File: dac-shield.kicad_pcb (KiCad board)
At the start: 2 copper layers, 53.3 x 53.3 mm, 40 parts, among them J1 Conn_01x02, J2 Conn_01x02, J3 Conn_01x02, J4 Conn_01x02, J5 Conn_01x02, J6 Conn_01x02, J7 Conn_01x02, J8 Conn_01x02

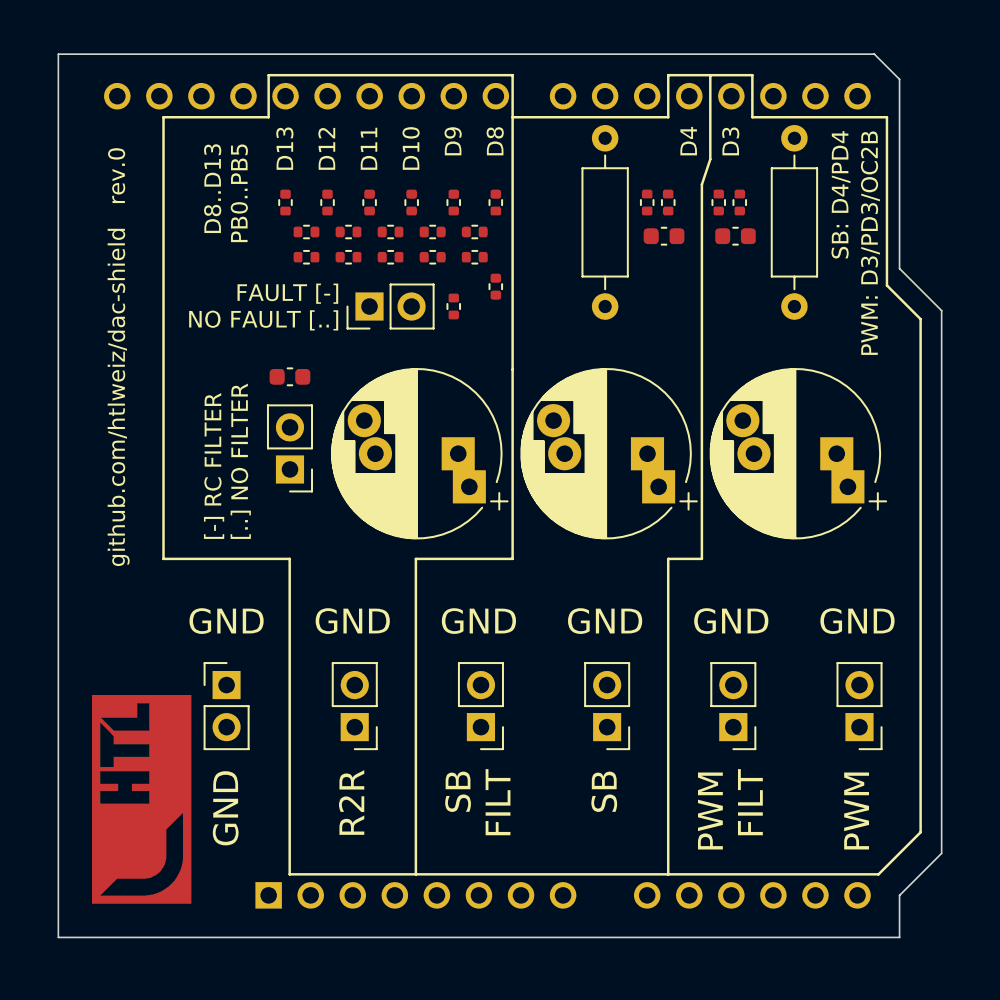
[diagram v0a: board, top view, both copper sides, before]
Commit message: modified silkscreen
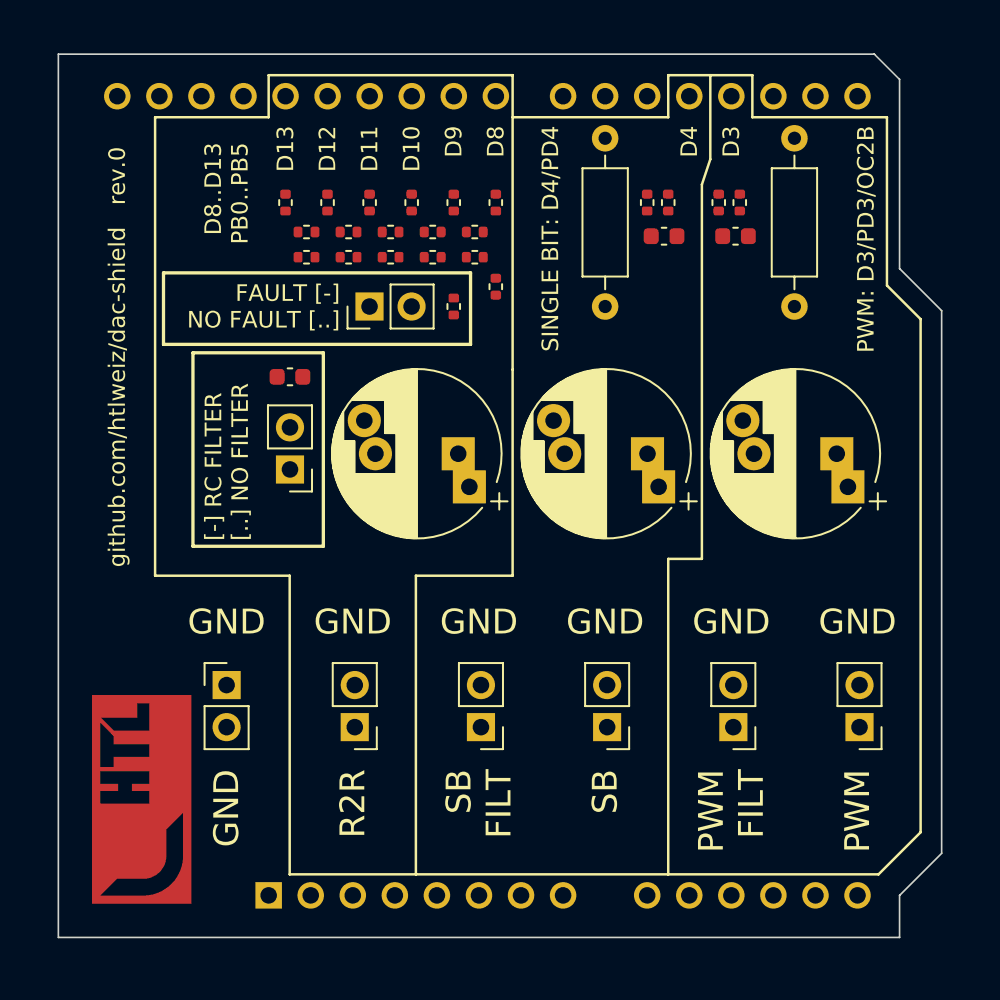
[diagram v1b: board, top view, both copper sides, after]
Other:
- board text added: "SINGLE BIT: D4/PD4"
- board text removed: "SB: D4/PD4"
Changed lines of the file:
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@@
   (gr_line (start 146.05 77.47) (end 148.59 77.47) (layer "F.SilkS") (width 0.15))
   (gr_line (start 161.29 92.202) (end 161.29 123.19) (layer "F.SilkS") (width 0.15))
-  (gr_line (start 136.652 106.68) (end 130.81 106.68) (layer "F.SilkS") (width 0.15))
+  (gr_line (start 136.652 107.696) (end 130.81 107.696) (layer "F.SilkS") (width 0.15))
   (gr_line (start 161.29 123.19) (end 158.75 125.73) (layer "F.SilkS") (width 0.15))
-  (gr_line (start 123.19 125.73) (end 123.19 106.68) (layer "F.SilkS") (width 0.15))
-  (gr_line (start 123.19 106.68) (end 115.57 106.68) (layer "F.SilkS") (width 0.15))
-  (gr_line (start 130.81 106.68) (end 130.81 125.73) (layer "F.SilkS") (width 0.15))
+  (gr_line (start 123.19 125.73) (end 123.19 107.696) (layer "F.SilkS") (width 0.15))
+  (gr_rect (start 115.57 89.408) (end 134.112 93.726) (layer "F.SilkS") (width 0.2) (fill none))
+  (gr_line (start 123.19 107.696) (end 115.062 107.696) (layer "F.SilkS") (width 0.15))
+  (gr_line (start 130.81 107.696) (end 130.81 125.73) (layer "F.SilkS") (width 0.15))
   (gr_line (start 158.75 125.73) (end 146.05 125.73) (layer "F.SilkS") (width 0.15))
   (gr_line (start 151.13 80.01) (end 159.258 80.01) (layer "F.SilkS") (width 0.15))
   (gr_line (start 159.258 90.17) (end 161.29 92.202) (layer "F.SilkS") (width 0.15))
   (gr_line (start 148.59 77.47) (end 148.59 82.55) (layer "F.SilkS") (width 0.15))
+  (gr_rect (start 117.348 105.918) (end 125.222 94.234) (layer "F.SilkS") (width 0.2) (fill none))
   (gr_line (start 136.652 77.47) (end 121.92 77.47) (layer "F.SilkS") (width 0.15))
   (gr_line (start 146.05 77.47) (end 146.05 80.01) (layer "F.SilkS") (width 0.15))
   (gr_line (start 146.05 106.68) (end 146.05 125.73) (layer "F.SilkS") (width 0.15))
-  (gr_line (start 115.57 80.01) (end 121.92 80.01) (layer "F.SilkS") (width 0.15))
-  (gr_line (start 136.652 95.25) (end 136.652 106.68) (layer "F.SilkS") (width 0.15))
-  (gr_line (start 115.57 106.68) (end 115.57 80.01) (layer "F.SilkS") (width 0.15))
+  (gr_line (start 115.062 80.01) (end 121.92 80.01) (layer "F.SilkS") (width 0.15))
+  (gr_line (start 136.652 95.25) (end 136.652 107.696) (layer "F.SilkS") (width 0.15))
+  (gr_line (start 115.062 107.696) (end 115.062 80.01) (layer "F.SilkS") (width 0.15))
   (gr_line (start 159.258 80.01) (end 159.258 90.17) (layer "F.SilkS") (width 0.15))
   (gr_line (start 148.082 106.68) (end 146.05 106.68) (layer "F.SilkS") (width 0.15))
@@
     (effects (font (size 1 1) (thickness 0.16)) (justify right))
   )
-  (gr_text "PWM: D3/PD3/OC2B" (at 158.242 80.772 90) (layer "F.SilkS")
+  (gr_text "PWM: D3/PD3/OC2B" (at 157.988 80.518 90) (layer "F.SilkS")
     (effects (font (size 1 1) (thickness 0.16)) (justify right))
   )
@@
     (effects (font (size 1 1) (thickness 0.16)) (justify right))
   )
-  (gr_text "SB: D4/PD4" (at 156.464 80.772 90) (layer "F.SilkS")
+  (gr_text "SINGLE BIT: D4/PD4" (at 138.938 80.518 90) (layer "F.SilkS")
     (effects (font (size 1 1) (thickness 0.16)) (justify right))
   )

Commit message: fixed cap value and added annotations
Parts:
- C1, C3, C5: value 16n -> 15n
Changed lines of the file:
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@@
   (net 31 "/pwm_filt")
   (net 32 "/sb_filt")
-  (net 33 "Net-(C6-Pad1)")
+  (net 33 "Net-(C5-Pad1)")
   (net 34 "Net-(J4-Pad1)")
   (net 35 "Net-(J4-Pad2)")
   (net 36 "/r2r_filt")
   (net 37 "Net-(R4-Pad2)")
-  (net 38 "Net-(R6-Pad2)")
-  (net 39 "Net-(R11-Pad2)")
+  (net 38 "Net-(R10-Pad1)")
+  (net 39 "Net-(R10-Pad2)")
   (net 40 "Net-(R19-Pad2)")
   (footprint "Resistor_SMD:R_0402_1005Metric" (layer "F.Cu")
@@
     (fp_circle (center 2.5 0) (end 7.5 0) (layer "F.Fab") (width 0.1) (fill none))
     (pad "1" thru_hole rect (at 0 0 180) (size 2 2) (drill 1) (layers *.Cu *.Mask)
-      (net 33 "Net-(C6-Pad1)") (pintype "passive"))
+      (net 33 "Net-(C5-Pad1)") (pintype "passive"))
     (pad "1" thru_hole rect (at -0.672144 -2 180) (size 2 2) (drill 1) (layers *.Cu *.Mask)
-      (net 33 "Net-(C6-Pad1)") (pintype "passive"))
+      (net 33 "Net-(C5-Pad1)") (pintype "passive"))
     (pad "2" thru_hole circle (at 5 0 180) (size 2 2) (drill 1) (layers *.Cu *.Mask)
       (net 6 "GND") (pintype "passive"))
@@
     (fp_line (start 0.525 0.27) (end -0.525 0.27) (layer "F.Fab") (width 0.1))
     (pad "1" smd roundrect (at -0.51 0 180) (size 0.54 0.64) (layers "F.Cu" "F.Paste" "F.Mask") (roundrect_rratio 0.25)
-      (net 39 "Net-(R11-Pad2)") (pintype "passive"))
+      (net 39 "Net-(R10-Pad2)") (pintype "passive"))
     (pad "2" smd roundrect (at 0.51 0 180) (size 0.54 0.64) (layers "F.Cu" "F.Paste" "F.Mask") (roundrect_rratio 0.25)
       (net 34 "Net-(J4-Pad1)") (pintype "passive"))
@@
       (effects (font (size 1 1) (thickness 0.15)))
     )
-    (fp_text value "16n" (at 0 1.43) (layer "F.Fab")
+    (fp_text value "15n" (at 0 1.43) (layer "F.Fab")
       (effects (font (size 1 1) (thickness 0.15)))
     )
@@
       (net 23 "/b1") (pintype "passive"))
     (pad "2" smd roundrect (at 0.51 0 270) (size 0.54 0.64) (layers "F.Cu" "F.Paste" "F.Mask") (roundrect_rratio 0.25)
-      (net 38 "Net-(R6-Pad2)") (pintype "passive"))
+      (net 38 "Net-(R10-Pad1)") (pintype "passive"))
     (model "${KICAD6_3DMODEL_DIR}/Resistor_SMD.3dshapes/R_0402_1005Metric.wrl"
       (offset (xyz 0 0 0))
@@
     (fp_line (start -0.525 0.27) (end -0.525 -0.27) (layer "F.Fab") (width 0.1))
     (pad "1" smd roundrect (at -0.51 0 270) (size 0.54 0.64) (layers "F.Cu" "F.Paste" "F.Mask") (roundrect_rratio 0.25)
-      (net 39 "Net-(R11-Pad2)") (pintype "passive"))
+      (net 39 "Net-(R10-Pad2)") (pintype "passive"))
     (pad "2" smd roundrect (at 0.51 0 270) (size 0.54 0.64) (layers "F.Cu" "F.Paste" "F.Mask") (roundrect_rratio 0.25)
       (net 35 "Net-(J4-Pad2)") (pintype "passive"))
@@
       (net 24 "/b2") (pintype "passive"))
     (pad "2" smd roundrect (at 0.51 0 270) (size 0.54 0.64) (layers "F.Cu" "F.Paste" "F.Mask") (roundrect_rratio 0.25)
-      (net 39 "Net-(R11-Pad2)") (pintype "passive"))
+      (net 39 "Net-(R10-Pad2)") (pintype "passive"))
     (model "${KICAD6_3DMODEL_DIR}/Resistor_SMD.3dshapes/R_0402_1005Metric.wrl"
       (offset (xyz 0 0 0))
@@
       (net 36 "/r2r_filt") (pinfunction "Pin_1") (pintype "passive"))
     (pad "2" thru_hole oval (at 0 2.54 180) (size 1.7 1.7) (drill 1) (layers *.Cu *.Mask)
-      (net 33 "Net-(C6-Pad1)") (pinfunction "Pin_2") (pintype "passive"))
+      (net 33 "Net-(C5-Pad1)") (pinfunction "Pin_2") (pintype "passive"))
     (model "${KICAD6_3DMODEL_DIR}/Connector_PinHeader_2.54mm.3dshapes/PinHeader_1x02_P2.54mm_Vertical.wrl"
       (offset (xyz 0 0 0))
@@
       (net 37 "Net-(R4-Pad2)") (pintype "passive"))
     (pad "2" smd roundrect (at 0.51 0 180) (size 0.54 0.64) (layers "F.Cu" "F.Paste" "F.Mask") (roundrect_rratio 0.25)
-      (net 38 "Net-(R6-Pad2)") (pintype "passive"))
+      (net 38 "Net-(R10-Pad1)") (pintype "passive"))
     (model "${KICAD6_3DMODEL_DIR}/Resistor_SMD.3dshapes/R_0402_1005Metric.wrl"
       (offset (xyz 0 0 0))
@@
     (fp_line (start 0.525 0.27) (end -0.525 0.27) (layer "F.Fab") (width 0.1))
     (pad "1" smd roundrect (at -0.51 0 180) (size 0.54 0.64) (layers "F.Cu" "F.Paste" "F.Mask") (roundrect_rratio 0.25)
-      (net 38 "Net-(R6-Pad2)") (pintype "passive"))
+      (net 38 "Net-(R10-Pad1)") (pintype "passive"))
     (pad "2" smd roundrect (at 0.51 0 180) (size 0.54 0.64) (layers "F.Cu" "F.Paste" "F.Mask") (roundrect_rratio 0.25)
-      (net 39 "Net-(R11-Pad2)") (pintype "passive"))
+      (net 39 "Net-(R10-Pad2)") (pintype "passive"))
     (model "${KICAD6_3DMODEL_DIR}/Resistor_SMD.3dshapes/R_0402_1005Metric.wrl"
       (offset (xyz 0 0 0))
@@
     (fp_line (start 0.525 0.27) (end -0.525 0.27) (layer "F.Fab") (width 0.1))
     (pad "1" smd roundrect (at -0.51 0 180) (size 0.54 0.64) (layers "F.Cu" "F.Paste" "F.Mask") (roundrect_rratio 0.25)
-      (net 38 "Net-(R6-Pad2)") (pintype "passive"))
+      (net 38 "Net-(R10-Pad1)") (pintype "passive"))
     (pad "2" smd roundrect (at 0.51 0 180) (size 0.54 0.64) (layers "F.Cu" "F.Paste" "F.Mask") (roundrect_rratio 0.25)
-      (net 39 "Net-(R11-Pad2)") (pintype "passive"))
+      (net 39 "Net-(R10-Pad2)") (pintype "passive"))
     (model "${KICAD6_3DMODEL_DIR}/Resistor_SMD.3dshapes/R_0402_1005Metric.wrl"
       (offset (xyz 0 0 0))
@@
       (effects (font (size 1 1) (thickness 0.15)))
     )
-    (fp_text value "16n" (at 0 1.43) (layer "F.Fab")
+    (fp_text value "15n" (at 0 1.43) (layer "F.Fab")
       (effects (font (size 1 1) (thickness 0.15)))
     )
@@
       (effects (font (size 1 1) (thickness 0.15)))
     )
-    (fp_text value "16n" (at 0 1.43) (layer "F.Fab")
+    (fp_text value "15n" (at 0 1.43) (layer "F.Fab")
       (effects (font (size 1 1) (thickness 0.15)))
     )
@@
     (fp_line (start 0.8 0.4) (end -0.8 0.4) (layer "F.Fab") (width 0.1))
     (pad "1" smd roundrect (at -0.775 0) (size 0.9 0.95) (layers "F.Cu" "F.Paste" "F.Mask") (roundrect_rratio 0.25)
-      (net 33 "Net-(C6-Pad1)") (pintype "passive"))
+      (net 33 "Net-(C5-Pad1)") (pintype "passive"))
     (pad "2" smd roundrect (at 0.775 0) (size 0.9 0.95) (layers "F.Cu" "F.Paste" "F.Mask") (roundrect_rratio 0.25)
       (net 6 "GND") (pintype "passive"))
@@
     (fp_line (start 0.525 -0.27) (end 0.525 0.27) (layer "F.Fab") (width 0.1))
     (pad "1" smd roundrect (at -0.51 0 180) (size 0.54 0.64) (layers "F.Cu" "F.Paste" "F.Mask") (roundrect_rratio 0.25)
-      (net 39 "Net-(R11-Pad2)") (pintype "passive"))
+      (net 39 "Net-(R10-Pad2)") (pintype "passive"))
     (pad "2" smd roundrect (at 0.51 0 180) (size 0.54 0.64) (layers "F.Cu" "F.Paste" "F.Mask") (roundrect_rratio 0.25)
       (net 34 "Net-(J4-Pad1)") (pintype "passive"))
@@
       (net 37 "Net-(R4-Pad2)") (pintype "passive"))
     (pad "2" smd roundrect (at 0.51 0 180) (size 0.54 0.64) (layers "F.Cu" "F.Paste" "F.Mask") (roundrect_rratio 0.25)
-      (net 38 "Net-(R6-Pad2)") (pintype "passive"))
+      (net 38 "Net-(R10-Pad1)") (pintype "passive"))
     (model "${KICAD6_3DMODEL_DIR}/Resistor_SMD.3dshapes/R_0402_1005Metric.wrl"
       (offset (xyz 0 0 0))

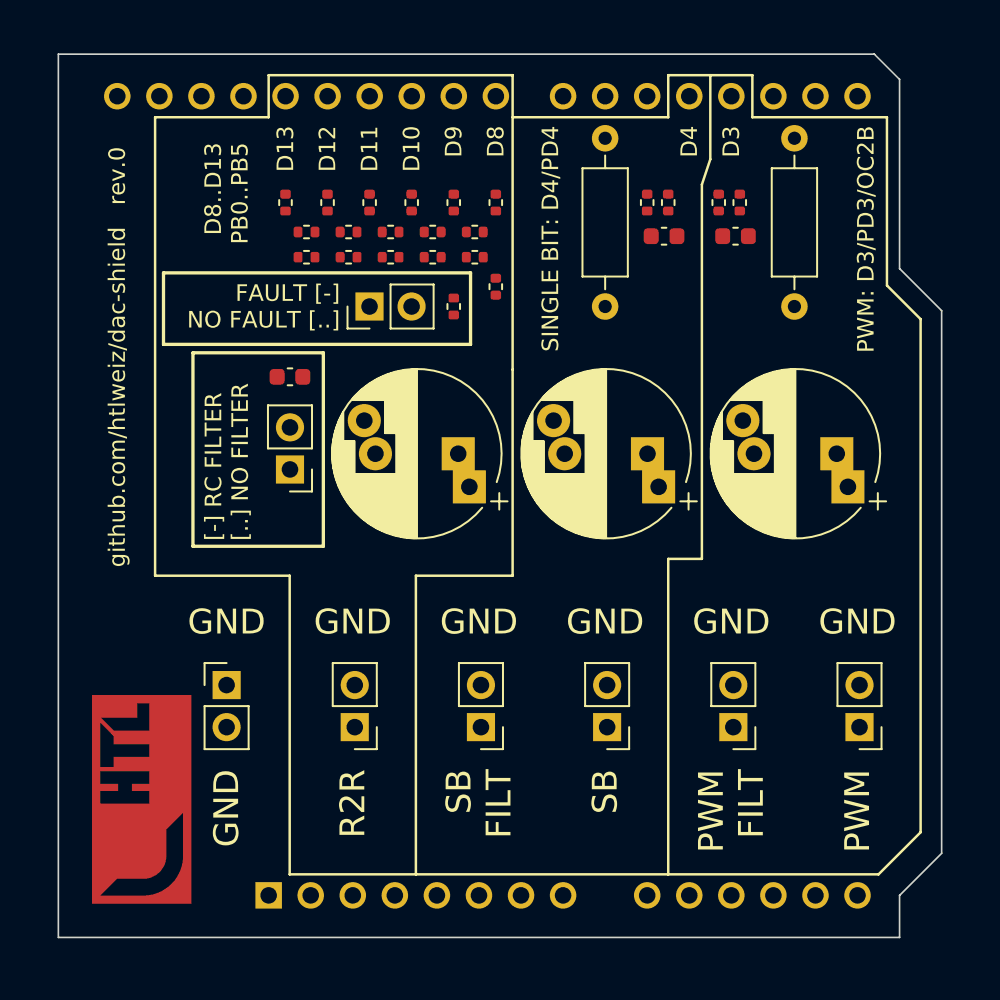
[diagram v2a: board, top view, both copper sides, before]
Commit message: added analog feedback
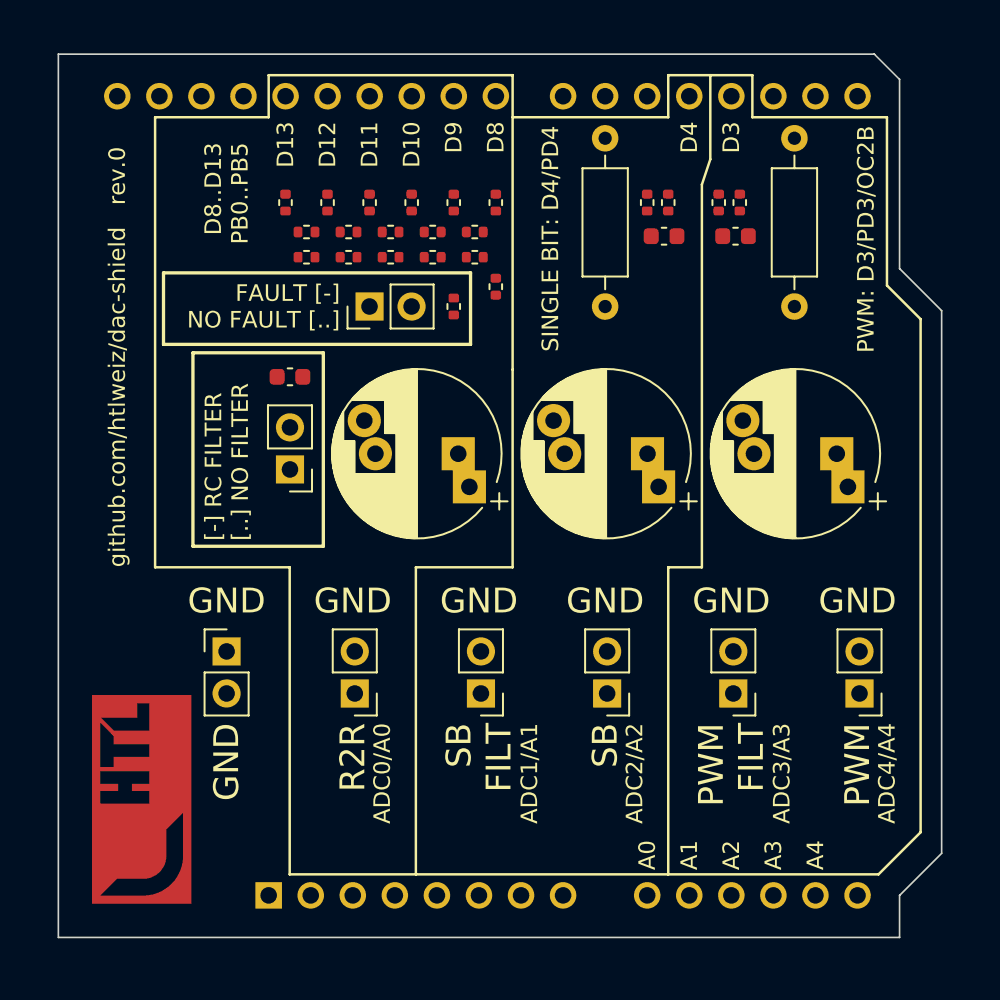
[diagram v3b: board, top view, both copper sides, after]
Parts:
- moved J1 2.03 mm to (157.6, 114.8)
- moved J2 2.03 mm to (150.0, 114.8)
- moved J3 2.03 mm to (142.4, 114.8)
- moved J5 2.03 mm to (134.7, 114.8)
- moved J7 2.03 mm to (127.1, 114.8)
- moved J8 2.03 mm to (119.4, 112.3)
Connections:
- A1 pad 10: unconnected-(A1-Pad10) -> sb_filt
- A1 pad 11: unconnected-(A1-Pad11) -> sb
- A1 pad 12: unconnected-(A1-Pad12) -> pwm_filt
- A1 pad 13: unconnected-(A1-Pad13) -> pwm
- A1 pad 18: /pwm -> pwm
- A1 pad 19: /sb -> sb
- A1 pad 9: unconnected-(A1-Pad9) -> r2r_filt
- C1 pad 1: /pwm_filt -> pwm_filt
- C2 pad 1: /pwm_filt -> pwm_filt
- C3 pad 1: /sb_filt -> sb_filt
- C4 pad 1: /sb_filt -> sb_filt
- J1 pad 1: /pwm -> pwm
- J2 pad 1: /pwm_filt -> pwm_filt
- J3 pad 1: /sb -> sb
- J5 pad 1: /sb_filt -> sb_filt
- J6 pad 1: /r2r_filt -> r2r_filt
- J7 pad 1: /r2r_filt -> r2r_filt
- R1 pad 1: /pwm -> pwm
- R1 pad 2: /pwm_filt -> pwm_filt
- R15 pad 1: /sb -> sb
- R15 pad 2: /sb_filt -> sb_filt
- R16 pad 1: /sb -> sb
- R16 pad 2: /sb_filt -> sb_filt
- R17 pad 1: /sb -> sb
- R17 pad 2: /sb_filt -> sb_filt
- R2 pad 1: /pwm -> pwm
- R2 pad 2: /pwm_filt -> pwm_filt
- R22 pad 2: /r2r_filt -> r2r_filt
- R23 pad 2: /r2r_filt -> r2r_filt
- R24 pad 2: /r2r_filt -> r2r_filt
- R3 pad 1: /pwm -> pwm
- R3 pad 2: /pwm_filt -> pwm_filt
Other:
- board text added: "A0"
- board text added: "A1"
- board text added: "A2"
- board text added: "A3"
- board text added: "A4"
- board text added: "ADC0/A0"
- board text added: "ADC1/A1"
- board text added: "ADC2/A2"
- board text added: "ADC3/A3"
- board text added: "ADC4/A4"

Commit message: first layout draft
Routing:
- net sb: track 0.00 -> 58.8 mm
- net pwm: track 0.00 -> 58.1 mm
- net r2r_filt: track 0.00 -> 58.1 mm
- net GND: track 0.00 -> 58.0 mm, vias 0 -> 31
- net sb_filt: track 0.00 -> 56.2 mm
- net pwm_filt: track 0.00 -> 48.3 mm
- net Net-(C5-Pad1): track 0.00 -> 15.7 mm
- net Net-(J4-Pad1): track 0.00 -> 9.50 mm
- net Net-(R10-Pad2): track 0.00 -> 9.41 mm
- net Net-(R10-Pad1): track 0.00 -> 6.21 mm
- net Net-(R19-Pad2): track 0.00 -> 6.21 mm
- net /b3: track 0.00 -> 5.92 mm
- net /b4: track 0.00 -> 5.92 mm
- net /b5: track 0.00 -> 5.92 mm
- net /b2: track 0.00 -> 5.92 mm
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- added copper zone on B.Cu, net GND
- added copper zone on F.Cu, net GND

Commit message: added test points, recreated fab files
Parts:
- added TP1: TestPoint_2Pole, TestPoint:TestPoint_2Pads_Pitch2.54mm_Drill0.8mm, F.Cu at (124.5, 114.8)
- added TP2: TestPoint_2Pole, TestPoint:TestPoint_2Pads_Pitch2.54mm_Drill0.8mm, F.Cu at (132.1, 114.8)
- added TP3: TestPoint_2Pole, TestPoint:TestPoint_2Pads_Pitch2.54mm_Drill0.8mm, F.Cu at (139.7, 114.8)
- added TP4: TestPoint_2Pole, TestPoint:TestPoint_2Pads_Pitch2.54mm_Drill0.8mm, F.Cu at (147.3, 114.8)
- added TP5: TestPoint_2Pole, TestPoint:TestPoint_2Pads_Pitch2.54mm_Drill0.8mm, F.Cu at (154.9, 114.8)
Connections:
- net /b0 renamed b0
- net /b1 renamed b1
- net /b2 renamed b2
- net /b3 renamed b3
- net /b4 renamed b4
- net /b5 renamed b5
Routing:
- net sb: track 58.8 -> 61.5 mm
- net sb_filt: track 56.2 -> 58.9 mm
- net pwm_filt: track 48.3 -> 51.0 mm
- net pwm: track 58.1 -> 60.8 mm
- net r2r_filt: track 58.1 -> 59.9 mm
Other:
- board text added: "ADC2/A2 D4"
- board text added: "ADC4/A4 D3"
- board text removed: "ADC2/A2"
- board text removed: "ADC4/A4"

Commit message: prettified things
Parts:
- added REF**: logo-6mm, htl-logos:logo-6mm, B.Cu at (139.8, 118.0)
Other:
- board text added: "PCB: wu@htlweiz.at"
